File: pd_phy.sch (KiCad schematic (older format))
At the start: 5 parts, among them U3 FUSB302B

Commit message: 4-layer board with smaller components
This is a major change!  Almost all the components have changed to
smaller versions, with 0603 and 0402 passives and a QFN microcontroller.
The board now has four layers, with internal layers used for VBUS and
GND.  The board now measures a mere 25×30 mm!  The SWD header and Boot
switch footprints have been moved to the bottom to help with this
shrinkage.  Two test points were added to the bottom as well to make it
possible to power the board without using the USB connector.  The
mounting holes are now slightly smaller (better sized for M3), and only
17 mm apart instead of the old 18 mm.

To sum up, everything is smaller and that's almost entirely a good
thing, except now it's not really possible to build one by hand.
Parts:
- C11, C12: footprint Capacitors_SMD:C_0805 -> Capacitors_SMD:C_0402
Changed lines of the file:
@@
 $Descr A4 11693 8268
 encoding utf-8
-Sheet 6 6
+Sheet 5 6
 Title "PD Buddy Sink"
 Date ""
@@
 $EndComp
 $Comp
-L VBUS #PWR026
+L VBUS #PWR028
 U 1 1 588FB397
 P 4800 3500
-F 0 "#PWR026" H 4800 3350 50  0001 C CNN
+F 0 "#PWR028" H 4800 3350 50  0001 C CNN
 F 1 "VBUS" H 4800 3640 50  0000 C CNN
 F 2 "" H 4800 3500 50  0000 C CNN
@@
 $EndComp
 $Comp
-L +3.3V #PWR027
+L +3.3V #PWR029
 U 1 1 588FB39E
 P 5200 3100
-F 0 "#PWR027" H 5200 2950 50  0001 C CNN
+F 0 "#PWR029" H 5200 2950 50  0001 C CNN
 F 1 "+3.3V" H 5200 3240 50  0000 C CNN
 F 2 "" H 5200 3100 50  0000 C CNN
@@
 $EndComp
 $Comp
-L GND #PWR028
+L GND #PWR030
 U 1 1 588FB3B4
 P 5300 4100
-F 0 "#PWR028" H 5300 3850 50  0001 C CNN
+F 0 "#PWR030" H 5300 3850 50  0001 C CNN
 F 1 "GND" H 5300 3950 50  0000 C CNN
 F 2 "" H 5300 4100 50  0000 C CNN
@@
 $EndComp
 $Comp
-L GND #PWR029
+L GND #PWR031
 U 1 1 588FB494
 P 4600 4100
-F 0 "#PWR029" H 4600 3850 50  0001 C CNN
+F 0 "#PWR031" H 4600 3850 50  0001 C CNN
 F 1 "GND" H 4600 3950 50  0000 C CNN
 F 2 "" H 4600 4100 50  0000 C CNN
@@
 $EndComp
 $Comp
-L GND #PWR030
+L GND #PWR032
 U 1 1 588FB4C0
 P 4300 4100
-F 0 "#PWR030" H 4300 3850 50  0001 C CNN
+F 0 "#PWR032" H 4300 3850 50  0001 C CNN
 F 1 "GND" H 4300 3950 50  0000 C CNN
 F 2 "" H 4300 4100 50  0000 C CNN
@@
 	5800 3500 5700 3500
 $Comp
-L +3.3V #PWR031
+L +3.3V #PWR033
 U 1 1 5892A15C
 P 6800 3200
-F 0 "#PWR031" H 6800 3050 50  0001 C CNN
+F 0 "#PWR033" H 6800 3050 50  0001 C CNN
 F 1 "+3.3V" H 6800 3340 50  0000 C CNN
 F 2 "" H 6800 3200 50  0000 C CNN
@@
 $EndComp
 $Comp
-L GND #PWR032
+L GND #PWR034
 U 1 1 5892A162
 P 6800 3900
-F 0 "#PWR032" H 6800 3650 50  0001 C CNN
+F 0 "#PWR034" H 6800 3650 50  0001 C CNN
 F 1 "GND" H 6800 3750 50  0000 C CNN
 F 2 "" H 6800 3900 50  0000 C CNN
@@
 F 0 "C11" H 6825 3650 50  0000 L CNN
 F 1 "0.1μF" H 6825 3450 50  0000 L CNN
-F 2 "Capacitors_SMD:C_0805" H 6838 3400 50  0001 C CNN
+F 2 "Capacitors_SMD:C_0402" H 6838 3400 50  0001 C CNN
 F 3 "" H 6800 3550 50  0000 C CNN
 	1    6800 3550
@@
 F 0 "C12" H 7225 3650 50  0000 L CNN
 F 1 "1μF" H 7225 3450 50  0000 L CNN
-F 2 "Capacitors_SMD:C_0805" H 7238 3400 50  0001 C CNN
+F 2 "Capacitors_SMD:C_0402" H 7238 3400 50  0001 C CNN
 F 3 "" H 7200 3550 50  0000 C CNN
 	1    7200 3550

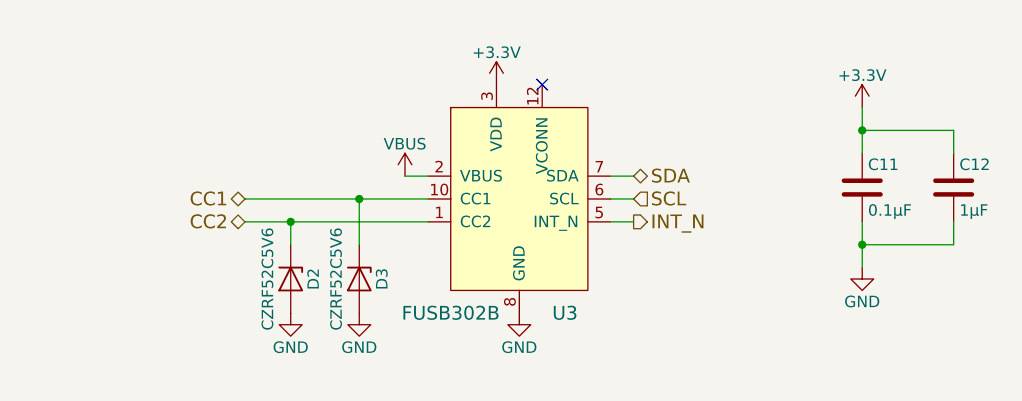
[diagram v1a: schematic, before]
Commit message: Use FUSB302BMPX from standard kicad-library
Now that the appropriate pull requests have been merged, I can use the
standard part rather than the one I created in this repository.
Speaking of which, this commit removes FUSB302B and MLP-14 from this
repository.
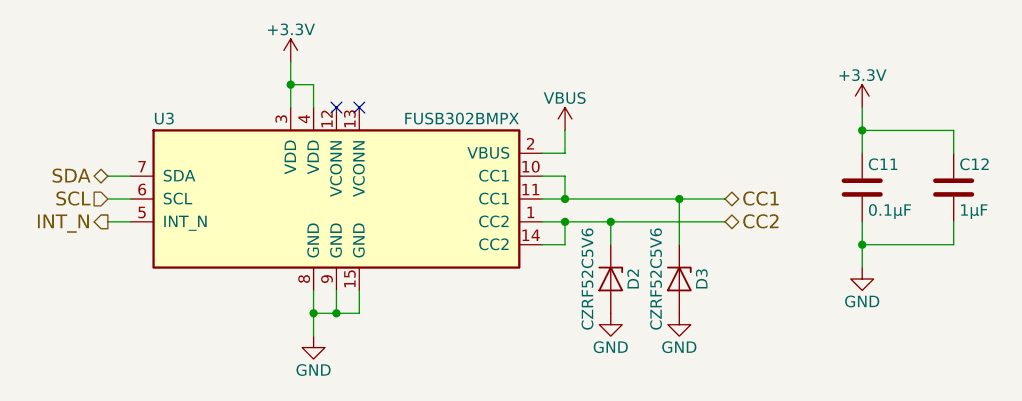
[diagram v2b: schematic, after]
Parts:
- removed U3: FUSB302B, pd-buddy:MLP-14, symbol FUSB302B
- added U3: FUSB302BMPX, Housings_DFN_QFN:Fairchild_MLP14D, symbol FUSB302BMPX
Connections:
- net +3V3: now also U3.3 (VDD), U3.4 (VDD)
- net CC1: now also U3.10 (CC1), U3.11 (CC1)
- net CC2: now also U3.1 (CC2), U3.14 (CC2)
- net GND: now also U3.15 (GND), U3.8 (GND), U3.9 (GND)
- net INT_N: now also U3.5 (INT_N)
- net SCL: now also U3.6 (SCL)
- net SDA: now also U3.7 (SDA)
- net VBUS: now also U3.2 (VBUS)
- no-connect marks 1 -> 2
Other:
- moved on the sheet: D2, D3
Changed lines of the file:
@@
 Comment4 "Based on AN-6102 (https://www.fairchildsemi.com/application-notes/AN/AN-6102.pdf)"
 $EndDescr
-$Comp
-L FUSB302B U3
-U 1 1 588FB390
-P 5300 3600
-F 0 "U3" H 5500 3100 60  0000 C CNN
-F 1 "FUSB302B" H 5000 3100 60  0000 C CNN
-F 2 "pd-buddy:MLP-14" H 5400 3000 60  0001 C CNN
-F 3 "https://www.fairchildsemi.com/datasheets/FU/FUSB302B.pdf" H 5500 3100 60  0001 C CNN
-	1    5300 3600
-	1    0    0    -1
-$EndComp
-$Comp
-L VBUS #PWR028
-U 1 1 588FB397
-P 4800 3500
-F 0 "#PWR028" H 4800 3350 50  0001 C CNN
-F 1 "VBUS" H 4800 3640 50  0000 C CNN
-F 2 "" H 4800 3500 50  0000 C CNN
-F 3 "" H 4800 3500 50  0000 C CNN
-	1    4800 3500
-	1    0    0    -1
-$EndComp
-$Comp
-L +3.3V #PWR029
-U 1 1 588FB39E
-P 5200 3100
-F 0 "#PWR029" H 5200 2950 50  0001 C CNN
-F 1 "+3.3V" H 5200 3240 50  0000 C CNN
-F 2 "" H 5200 3100 50  0000 C CNN
-F 3 "" H 5200 3100 50  0000 C CNN
-	1    5200 3100
-	1    0    0    -1
-$EndComp
-$Comp
-L GND #PWR030
-U 1 1 588FB3B4
-P 5300 4100
-F 0 "#PWR030" H 5300 3850 50  0001 C CNN
-F 1 "GND" H 5300 3950 50  0000 C CNN
-F 2 "" H 5300 4100 50  0000 C CNN
-F 3 "" H 5300 4100 50  0000 C CNN
-	1    5300 4100
-	1    0    0    -1
-$EndComp
-Text HLabel 4100 3600 0    60   BiDi ~ 0
+Text HLabel 6200 3600 2    60   BiDi ~ 0
 CC1
-Text HLabel 4100 3700 0    60   BiDi ~ 0
+Text HLabel 6200 3700 2    60   BiDi ~ 0
 CC2
 $Comp
 L D_Zener D2
 U 1 1 588FB3E3
-P 4300 3950
-F 0 "D2" H 4300 4050 50  0000 C CNN
-F 1 "CZRF52C5V6" H 4300 3850 50  0000 C CNN
-F 2 "Diodes_SMD:D_SOD-323" H 4300 3950 50  0001 C CNN
-F 3 "" H 4300 3950 50  0000 C CNN
-	1    4300 3950
+P 5700 3950
+F 0 "D2" H 5700 4050 50  0000 C CNN
+F 1 "CZRF52C5V6" H 5700 3850 50  0000 C CNN
+F 2 "Diodes_SMD:D_SOD-323" H 5700 3950 50  0001 C CNN
+F 3 "" H 5700 3950 50  0000 C CNN
+	1    5700 3950
 	0    1    1    0
 $EndComp
 $Comp
-L GND #PWR031
+L GND #PWR028
 U 1 1 588FB494
-P 4600 4100
-F 0 "#PWR031" H 4600 3850 50  0001 C CNN
-F 1 "GND" H 4600 3950 50  0000 C CNN
-F 2 "" H 4600 4100 50  0000 C CNN
-F 3 "" H 4600 4100 50  0000 C CNN
-	1    4600 4100
-	1    0    0    -1
-$EndComp
-$Comp
-L GND #PWR032
+P 6000 4100
+F 0 "#PWR028" H 6000 3850 50  0001 C CNN
+F 1 "GND" H 6000 3950 50  0000 C CNN
+F 2 "" H 6000 4100 50  0000 C CNN
+F 3 "" H 6000 4100 50  0000 C CNN
+	1    6000 4100
+	1    0    0    -1
+$EndComp
+$Comp
+L GND #PWR029
 U 1 1 588FB4C0
-P 4300 4100
-F 0 "#PWR032" H 4300 3850 50  0001 C CNN
-F 1 "GND" H 4300 3950 50  0000 C CNN
-F 2 "" H 4300 4100 50  0000 C CNN
-F 3 "" H 4300 4100 50  0000 C CNN
-	1    4300 4100
+P 5700 4100
+F 0 "#PWR029" H 5700 3850 50  0001 C CNN
+F 1 "GND" H 5700 3950 50  0000 C CNN
+F 2 "" H 5700 4100 50  0000 C CNN
+F 3 "" H 5700 4100 50  0000 C CNN
+	1    5700 4100
 	1    0    0    -1
 $EndComp
@@
 L D_Zener D3
 U 1 1 588FB500
-P 4600 3950
-F 0 "D3" H 4600 4050 50  0000 C CNN
-F 1 "CZRF52C5V6" H 4600 3850 50  0000 C CNN
-F 2 "Diodes_SMD:D_SOD-323" H 4600 3950 50  0001 C CNN
-F 3 "" H 4600 3950 50  0000 C CNN
-	1    4600 3950
+P 6000 3950
+F 0 "D3" H 6000 4050 50  0000 C CNN
+F 1 "CZRF52C5V6" H 6000 3850 50  0000 C CNN
+F 2 "Diodes_SMD:D_SOD-323" H 6000 3950 50  0001 C CNN
+F 3 "" H 6000 3950 50  0000 C CNN
+	1    6000 3950
 	0    1    1    0
 $EndComp
-Text HLabel 5800 3500 2    60   BiDi ~ 0
+Text HLabel 3500 3500 0    60   BiDi ~ 0
 SDA
-Text HLabel 5800 3600 2    60   Input ~ 0
+Text HLabel 3500 3600 0    60   Input ~ 0
 SCL
-Text HLabel 5800 3700 2    60   Output ~ 0
+Text HLabel 3500 3700 0    60   Output ~ 0
 INT_N
-Wire Wire Line
-	4800 3500 4900 3500
-Wire Wire Line
-	4100 3600 4900 3600
-Wire Wire Line
-	4100 3700 4900 3700
-Wire Wire Line
-	4300 3800 4300 3700
-Connection ~ 4300 3700
-Wire Wire Line
-	4600 3800 4600 3600
-Connection ~ 4600 3600
-Wire Wire Line
-	5800 3700 5700 3700
-Wire Wire Line
-	5700 3600 5800 3600
-Wire Wire Line
-	5800 3500 5700 3500
-$Comp
-L +3.3V #PWR033
+$Comp
+L +3.3V #PWR030
 U 1 1 5892A15C
 P 6800 3200
-F 0 "#PWR033" H 6800 3050 50  0001 C CNN
+F 0 "#PWR030" H 6800 3050 50  0001 C CNN
 F 1 "+3.3V" H 6800 3340 50  0000 C CNN
 F 2 "" H 6800 3200 50  0000 C CNN
@@
 $EndComp
 $Comp
-L GND #PWR034
+L GND #PWR031
 U 1 1 5892A162
 P 6800 3900
-F 0 "#PWR034" H 6800 3650 50  0001 C CNN
+F 0 "#PWR031" H 6800 3650 50  0001 C CNN
 F 1 "GND" H 6800 3750 50  0000 C CNN
 F 2 "" H 6800 3900 50  0000 C CNN
@@
 	1    0    0    -1
 $EndComp
-Wire Wire Line
-	6800 3200 6800 3400
-Wire Wire Line
-	6800 3700 6800 3900
-Wire Wire Line
-	6800 3800 7200 3800
-Wire Wire Line
-	7200 3800 7200 3700
-Connection ~ 6800 3800
-Wire Wire Line
-	7200 3400 7200 3300
-Wire Wire Line
-	7200 3300 6800 3300
-Connection ~ 6800 3300
 $Comp
 L C C12
@@
 	1    0    0    -1
 $EndComp
-NoConn ~ 5400 3100
+$Comp
+L FUSB302BMPX U3
+U 1 1 590DF24A
+P 4500 3600
+F 0 "U3" H 3700 3950 50  0000 L CNN
+F 1 "FUSB302BMPX" H 5300 3950 50  0000 R CNN
+F 2 "Housings_DFN_QFN:Fairchild_MLP14D" H 4500 3100 50  0001 C CNN
+F 3 "" H 4600 3200 50  0001 C CNN
+	1    4500 3600
+	1    0    0    -1
+$EndComp
+NoConn ~ 4500 3200
+NoConn ~ 4600 3200
+$Comp
+L +3.3V #PWR032
+U 1 1 590DF433
+P 4300 3000
+F 0 "#PWR032" H 4300 2850 50  0001 C CNN
+F 1 "+3.3V" H 4300 3140 50  0000 C CNN
+F 2 "" H 4300 3000 50  0000 C CNN
+F 3 "" H 4300 3000 50  0000 C CNN
+	1    4300 3000
+	1    0    0    -1
+$EndComp
+$Comp
+L GND #PWR033
+U 1 1 590DF4A2
+P 4400 4200
+F 0 "#PWR033" H 4400 3950 50  0001 C CNN
+F 1 "GND" H 4400 4050 50  0000 C CNN
+F 2 "" H 4400 4200 50  0000 C CNN
+F 3 "" H 4400 4200 50  0000 C CNN
+	1    4400 4200
+	1    0    0    -1
+$EndComp
+$Comp
+L VBUS #PWR034
+U 1 1 590DF5B0
+P 5500 3300
+F 0 "#PWR034" H 5500 3150 50  0001 C CNN
+F 1 "VBUS" H 5500 3440 50  0000 C CNN
+F 2 "" H 5500 3300 50  0000 C CNN
+F 3 "" H 5500 3300 50  0000 C CNN
+	1    5500 3300
+	1    0    0    -1
+$EndComp
+Wire Wire Line
+	5400 3600 6200 3600
+Wire Wire Line
+	5400 3700 6200 3700
+Wire Wire Line
+	5700 3800 5700 3700
+Connection ~ 5700 3700
+Wire Wire Line
+	6000 3800 6000 3600
+Connection ~ 6000 3600
+Wire Wire Line
+	3600 3700 3500 3700
+Wire Wire Line
+	3500 3600 3600 3600
+Wire Wire Line
+	3600 3500 3500 3500
+Wire Wire Line
+	6800 3200 6800 3400
+Wire Wire Line
+	6800 3700 6800 3900
+Wire Wire Line
+	6800 3800 7200 3800
+Wire Wire Line
+	7200 3800 7200 3700
+Connection ~ 6800 3800
+Wire Wire Line
+	7200 3400 7200 3300
+Wire Wire Line
+	7200 3300 6800 3300
+Connection ~ 6800 3300
+Wire Wire Line
+	4300 3000 4300 3200
+Wire Wire Line
+	4300 3100 4400 3100
+Wire Wire Line
+	4400 3100 4400 3200
+Connection ~ 4300 3100
+Wire Wire Line
+	4400 4000 4400 4200
+Wire Wire Line
+	4400 4100 4600 4100
+Wire Wire Line
+	4500 4100 4500 4000
+Connection ~ 4400 4100
+Wire Wire Line
+	4600 4100 4600 4000
+Connection ~ 4500 4100
+Wire Wire Line
+	5400 3400 5500 3400
+Wire Wire Line
+	5500 3400 5500 3300
+Wire Wire Line
+	5500 3700 5500 3800
+Wire Wire Line
+	5500 3800 5400 3800
+Wire Wire Line
+	5500 3600 5500 3500
+Wire Wire Line
+	5500 3500 5400 3500
+Connection ~ 5500 3600
+Connection ~ 5500 3700
 $EndSCHEMATC

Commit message: SOD-323F footprint for D2 and D3
KiCad has the right footprint now, so I don't have to substitute an
SOD-323 footprint.  The 3D model looks less inaccurate I suppose, but
still not right for the particular diodes I'm using.
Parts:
- D2, D3: footprint Diodes_SMD:D_SOD-323 -> Diodes_SMD:D_SOD-323F
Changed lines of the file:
@@
 F 0 "D2" H 5700 4050 50  0000 C CNN
 F 1 "CZRF52C5V6" H 5700 3850 50  0000 C CNN
-F 2 "Diodes_SMD:D_SOD-323" H 5700 3950 50  0001 C CNN
-F 3 "" H 5700 3950 50  0000 C CNN
+F 2 "Diodes_SMD:D_SOD-323F" H 5700 3950 50  0001 C CNN
+F 3 "http://www.comchiptech.com/cms/UserFiles/CZRF52C2-HF%20Thru.%20CZRF52C39-HF%20RevB.pdf" H 5700 3950 50  0001 C CNN
 	1    5700 3950
 	0    1    1    0
@@
 F 0 "D3" H 6000 4050 50  0000 C CNN
 F 1 "CZRF52C5V6" H 6000 3850 50  0000 C CNN
-F 2 "Diodes_SMD:D_SOD-323" H 6000 3950 50  0001 C CNN
-F 3 "" H 6000 3950 50  0000 C CNN
+F 2 "Diodes_SMD:D_SOD-323F" H 6000 3950 50  0001 C CNN
+F 3 "http://www.comchiptech.com/cms/UserFiles/CZRF52C2-HF%20Thru.%20CZRF52C39-HF%20RevB.pdf" H 6000 3950 50  0001 C CNN
 	1    6000 3950
 	0    1    1    0

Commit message: Change part for D2 and D3
Now they're MM3Z5V6T1G, an SOD-323 5.6 V 300 mW Zener diode.  Similar to
the old part, but easier to solder and cheaper.  One of those two points
matters.
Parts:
- D2, D3: value CZRF52C5V6 -> MM3Z5V6T1G; footprint Diodes_SMD:D_SOD-323F -> Diodes_SMD:D_SOD-323
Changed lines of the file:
@@
 P 5700 3950
 F 0 "D2" H 5700 4050 50  0000 C CNN
-F 1 "CZRF52C5V6" H 5700 3850 50  0000 C CNN
-F 2 "Diodes_SMD:D_SOD-323F" H 5700 3950 50  0001 C CNN
-F 3 "http://www.comchiptech.com/cms/UserFiles/CZRF52C2-HF%20Thru.%20CZRF52C39-HF%20RevB.pdf" H 5700 3950 50  0001 C CNN
+F 1 "MM3Z5V6T1G" H 5700 3850 50  0000 C CNN
+F 2 "Diodes_SMD:D_SOD-323" H 5700 3950 50  0001 C CNN
+F 3 "https://www.onsemi.com/pub/Collateral/MM3Z2V4T1-D.PDF" H 5700 3950 50  0001 C CNN
 	1    5700 3950
 	0    1    1    0
@@
 P 6000 3950
 F 0 "D3" H 6000 4050 50  0000 C CNN
-F 1 "CZRF52C5V6" H 6000 3850 50  0000 C CNN
-F 2 "Diodes_SMD:D_SOD-323F" H 6000 3950 50  0001 C CNN
-F 3 "http://www.comchiptech.com/cms/UserFiles/CZRF52C2-HF%20Thru.%20CZRF52C39-HF%20RevB.pdf" H 6000 3950 50  0001 C CNN
+F 1 "MM3Z5V6T1G" H 6000 3850 50  0000 C CNN
+F 2 "Diodes_SMD:D_SOD-323" H 6000 3950 50  0001 C CNN
+F 3 "https://www.onsemi.com/pub/Collateral/MM3Z2V4T1-D.PDF" H 6000 3950 50  0001 C CNN
 	1    6000 3950
 	0    1    1    0
